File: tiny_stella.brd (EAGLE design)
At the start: 99.7 x 85.1 mm, 84 parts, among them IC1 74LS00D, SW1 RGT_DIFFICULTY, SW2 LFT_DIFFICULTY, SW3 ON/OFF, SW4 ON/OFF, T1 2N3904, T2 PN3906, T3 PN3906, T4 PN3906, X1 SSW-112-02-G-Q

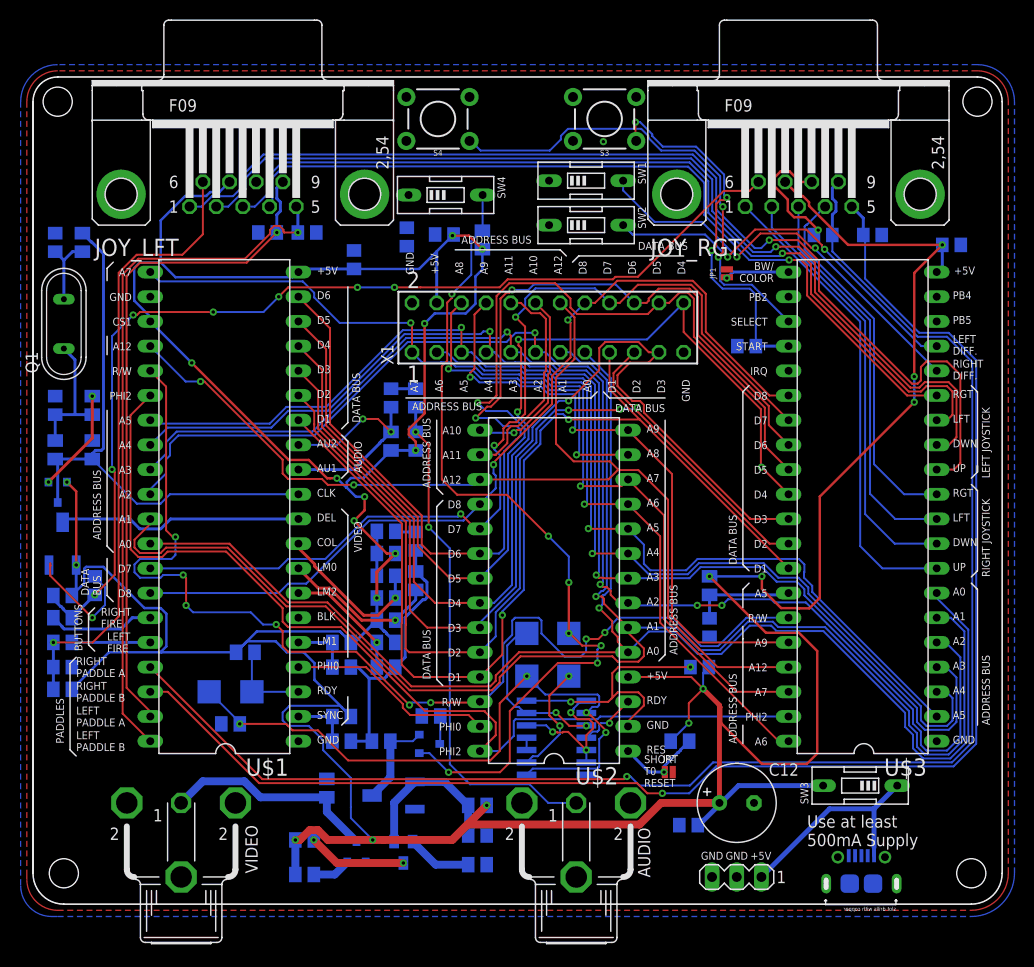
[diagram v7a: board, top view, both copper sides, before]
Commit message: swapped the left and right joystick inputs'
'
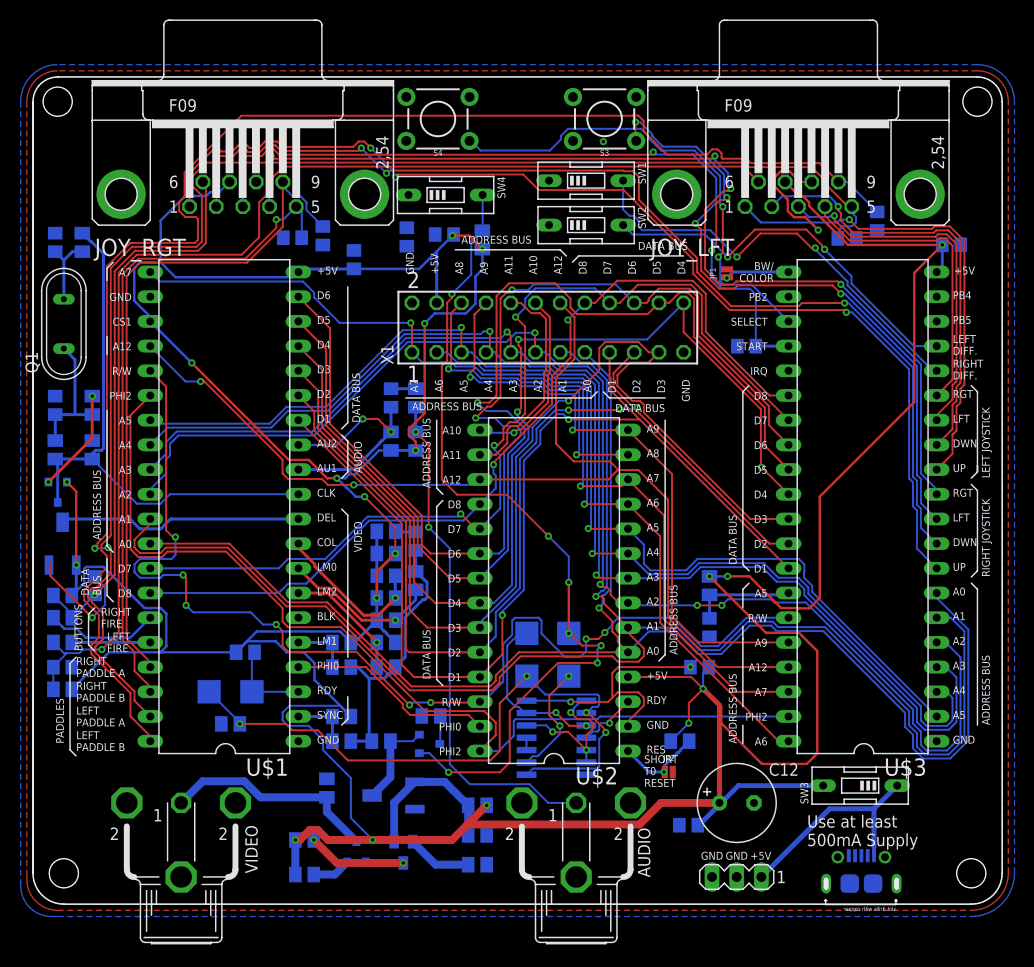
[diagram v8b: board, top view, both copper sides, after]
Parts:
- moved C8 62.7 mm to (86.8, 70.3), turned to 270 degrees
- moved C6 59.7 mm to (26.7, 68.6), turned to 0 degrees
- moved JOY_LFT 57.1 mm to (78.7, 73.0)
- moved JOY_RGT 57.1 mm to (21.6, 73.0)
- moved C9 55.6 mm to (83.7, 68.5)
- moved C7 51.5 mm to (29.8, 68.8), turned to 270 degrees
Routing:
- net RGT_PADDLE_A: track 157.6 -> 70.8 mm, vias 1 -> 0
- net RGT_PADDLE_B: track 153.7 -> 68.8 mm
- net LFT_PADDLE_A: track 69.4 -> 151.2 mm, vias 1 -> 2
- net LFT_PADDLE_B: track 72.7 -> 146.6 mm, vias 1 -> 0
- net RGT_JOY_LFT: track 40.5 -> 109.5 mm, vias 0 -> 4
- net RGT_JOY_RGT: track 38.1 -> 105.4 mm, vias 0 -> 4
- net RGT_JOY_DWN: track 44.2 -> 109.1 mm, vias 0 -> 5
- net RGT_JOY_UP: track 48.6 -> 112.4 mm, vias 0 -> 3
- net LFT_JOY_UP: track 110.5 -> 49.2 mm
- net N$10: track 63.7 -> 123.1 mm
- net LFT_JOY_LFT: track 94.4 -> 37.3 mm
- net LFT_JOY_DWN: track 100.6 -> 44.6 mm
- net LFT_JOY_RGT: track 85.4 -> 31.6 mm, vias 1 -> 0
- net N$9: track 107.1 -> 57.5 mm, vias 7 -> 1
- net +5V: track 471.5 -> 466.9 mm, vias 22 -> 19
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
